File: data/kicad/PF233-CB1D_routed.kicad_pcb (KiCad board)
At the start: 6 copper layers, 78 x 77.2 mm, 61 parts, among them M5 5 V 1.5 A switching module, U1 Pico 2 W

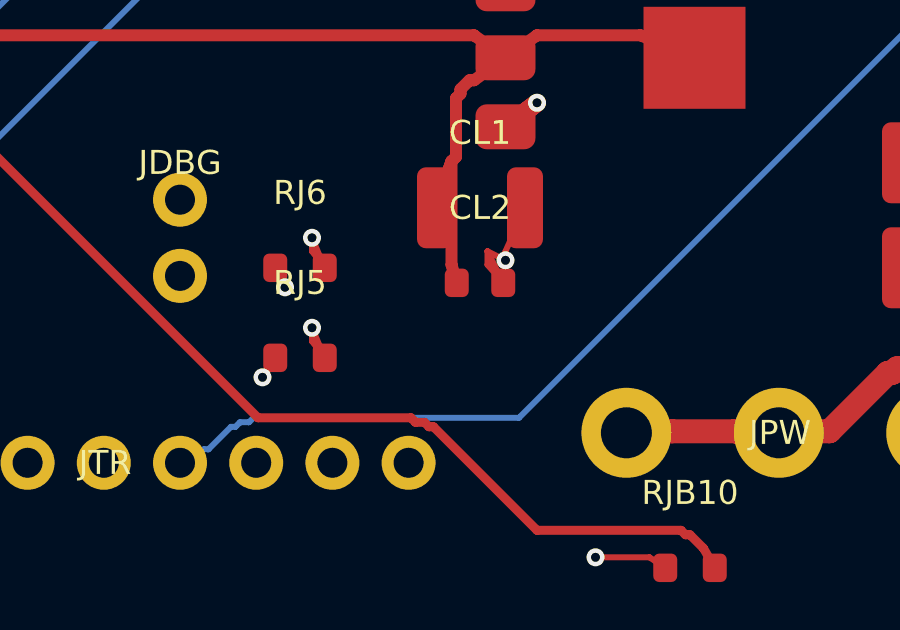
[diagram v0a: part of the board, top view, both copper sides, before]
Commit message: WIP stage 5: B3/B5/B6/B8 closed in blockers.json, B7 narrowed to HVTERM, B12 opened; cap-v18 pipeline step (cap was not regenerated on a fresh work/); upper_check septum joint by voxels; curated STLs refreshed (U6 dock for the real MT60, septum lap segments, canonical face order); DESIGN_STATE stress counts
Co-Authored-By: Claude Opus 5.5 <noreply@anthropic.com>
Claude-Session: https://claude.ai/code/session_01FX4DWSYYjMCFGGA6gmha65
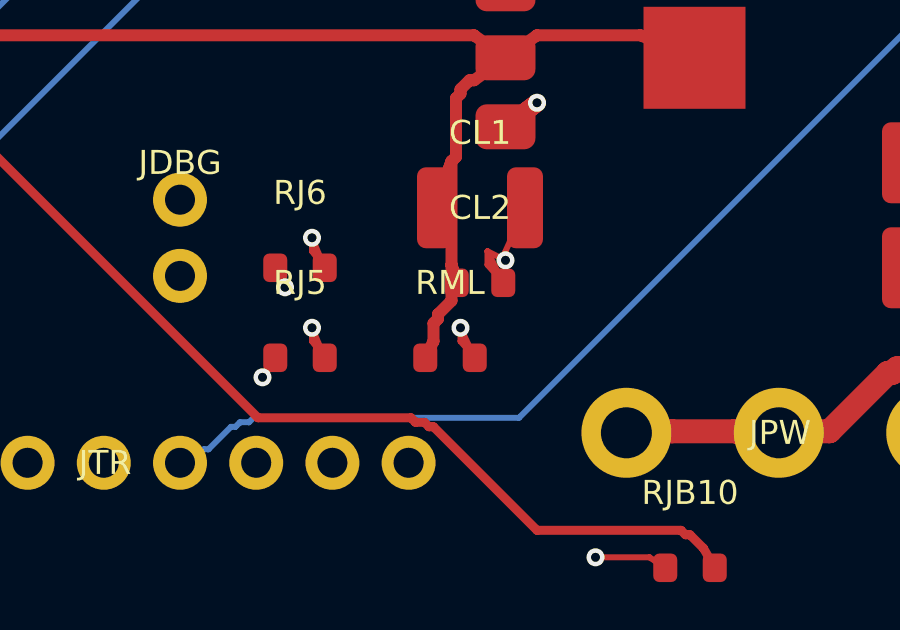
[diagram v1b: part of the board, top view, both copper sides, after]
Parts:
- added RML: 270, Resistor_SMD:R_0603_1608Metric, F.Cu at (97.0, 124.0)
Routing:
- net +3V3D: track 68.7 -> 72.7 mm
- net GND: track 106.4 -> 108.7 mm, vias 38 -> 39
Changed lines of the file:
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@@
     (pad "2" smd roundrect (at 0.775 0.000) (size 0.800 0.950) (layers "F.Cu" "F.Paste" "F.Mask") (net 13 "GND"))
+  )
+  (footprint "Resistor_SMD:R_0603_1608Metric" (layer "F.Cu") (at 97.0000 124.0000)
+    (property "Reference" "RML" (at 0 -2.5 0) (layer "F.SilkS") (effects (font (size 0.8 0.8) (thickness 0.12))))
+    (property "Value" "270" (at 0 2.5 0) (layer "F.Fab") (effects (font (size 0.8 0.8) (thickness 0.12))))
+    (attr smd)
+    (model "${KIPRJMOD}/3dmodels/PF233_R0603.wrl" (offset (xyz 0 0 0)) (scale (xyz 0.3937 0.3937 0.3937)) (rotate (xyz 0 0 0)))
+    (pad "1" smd roundrect (at -0.825 0.000) (size 0.800 0.950) (layers "F.Cu" "F.Paste" "F.Mask") (net 1 "+3V3D"))
+    (pad "2" smd roundrect (at 0.825 0.000) (size 0.800 0.950) (layers "F.Cu" "F.Paste" "F.Mask") (net 13 "GND"))
   )
   (footprint "Package_SO:SOIC-16_3.9x9.9mm_P1.27mm" (layer "F.Cu") (at 97.0000 100.0000)
@@
   (segment (start 98.2500 120.9000) (end 98.2500 120.4500) (width 0.2) (layer "F.Cu") (net 13))
   (segment (start 98.2500 120.4500) (end 98.7750 121.5000) (width 0.2) (layer "F.Cu") (net 13))
+  (segment (start 97.8250 124.0000) (end 97.3500 123.4500) (width 0.2) (layer "F.Cu") (net 13))
+  (segment (start 97.3500 123.4500) (end 97.3500 123.0000) (width 0.2) (layer "F.Cu") (net 13))
+  (segment (start 97.3500 123.0000) (end 97.8250 124.0000) (width 0.2) (layer "F.Cu") (net 13))
   (segment (start 94.3000 96.8250) (end 93.4500 96.6000) (width 0.2) (layer "F.Cu") (net 13))
   (segment (start 93.4500 96.6000) (end 93.0000 96.6000) (width 0.2) (layer "F.Cu") (net 13))
@@
   (segment (start 97.0500 117.4500) (end 97.0500 120.9000) (width 0.4) (layer "F.Cu") (net 1))
   (segment (start 97.0500 120.9000) (end 97.2250 121.5000) (width 0.4) (layer "F.Cu") (net 1))
+  (segment (start 97.2250 121.5000) (end 97.0500 120.9000) (width 0.4) (layer "F.Cu") (net 1))
+  (segment (start 97.0500 120.9000) (end 97.0500 122.1000) (width 0.4) (layer "F.Cu") (net 1))
+  (segment (start 97.0500 122.1000) (end 96.6000 122.5500) (width 0.4) (layer "F.Cu") (net 1))
+  (segment (start 96.6000 122.5500) (end 96.6000 122.7000) (width 0.4) (layer "F.Cu") (net 1))
+  (segment (start 96.6000 122.7000) (end 96.4500 122.8500) (width 0.4) (layer "F.Cu") (net 1))
+  (segment (start 96.4500 122.8500) (end 96.4500 123.4500) (width 0.4) (layer "F.Cu") (net 1))
+  (segment (start 96.4500 123.4500) (end 96.1750 124.0000) (width 0.4) (layer "F.Cu") (net 1))
   (segment (start 98.8500 114.0000) (end 97.8000 113.2500) (width 0.4) (layer "F.Cu") (net 1))
   (segment (start 97.8000 113.2500) (end 78.9000 113.2500) (width 0.4) (layer "F.Cu") (net 1))
@@
   (via (at 97.3500 111.0000) (size 0.6) (drill 0.3) (layers "F.Cu" "B.Cu") (net 13))
   (via (at 98.8500 120.7500) (size 0.6) (drill 0.3) (layers "F.Cu" "B.Cu") (net 13))
+  (via (at 97.3500 123.0000) (size 0.6) (drill 0.3) (layers "F.Cu" "B.Cu") (net 13))
   (via (at 93.0000 96.6000) (size 0.6) (drill 0.3) (layers "F.Cu" "B.Cu") (net 13))
   (via (at 93.0000 99.0000) (size 0.6) (drill 0.3) (layers "F.Cu" "B.Cu") (net 13))

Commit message: WIP: sign-off re-run outputs (publish in progress)
Co-Authored-By: Claude Opus 5.5 <noreply@anthropic.com>
Claude-Session: https://claude.ai/code/session_01FX4DWSYYjMCFGGA6gmha65
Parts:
- JLB: value to LB1: +5V, LED_IN, GND, GND -> to LB1: +5V, LED_IN, LED_CLK, GND
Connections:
- JLB pad 3: GND -> LED_CLK
- U1 pad 19: (no net) -> LED_CLK
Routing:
- net LED_CLK: track 0.00 -> 52.5 mm
- net UMB_SHLD: track 99.1 -> 102.3 mm
- net DIAL_EXT: track 74.2 -> 76.1 mm
- net TRIG_EXT: track 79.8 -> 78.6 mm, vias 1 -> 2
- net SHIELD: track 58.4 -> 57.2 mm, vias 2 -> 3
- net JB10_VCM: track 45.1 -> 44.8 mm, vias 1 -> 2
- net VBUS_SENSE: vias 3 -> 4
